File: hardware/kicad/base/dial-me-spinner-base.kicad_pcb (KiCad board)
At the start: 2 copper layers, 57.6 x 46 mm, 25 parts, among them J1 TYPE-C-31-M-12, J2 BATT, J3 LINK, Q1 BSS138DW, SW1 TS-1187A, U1 BQ25180YBGR, U2 USBLC6-2SC6

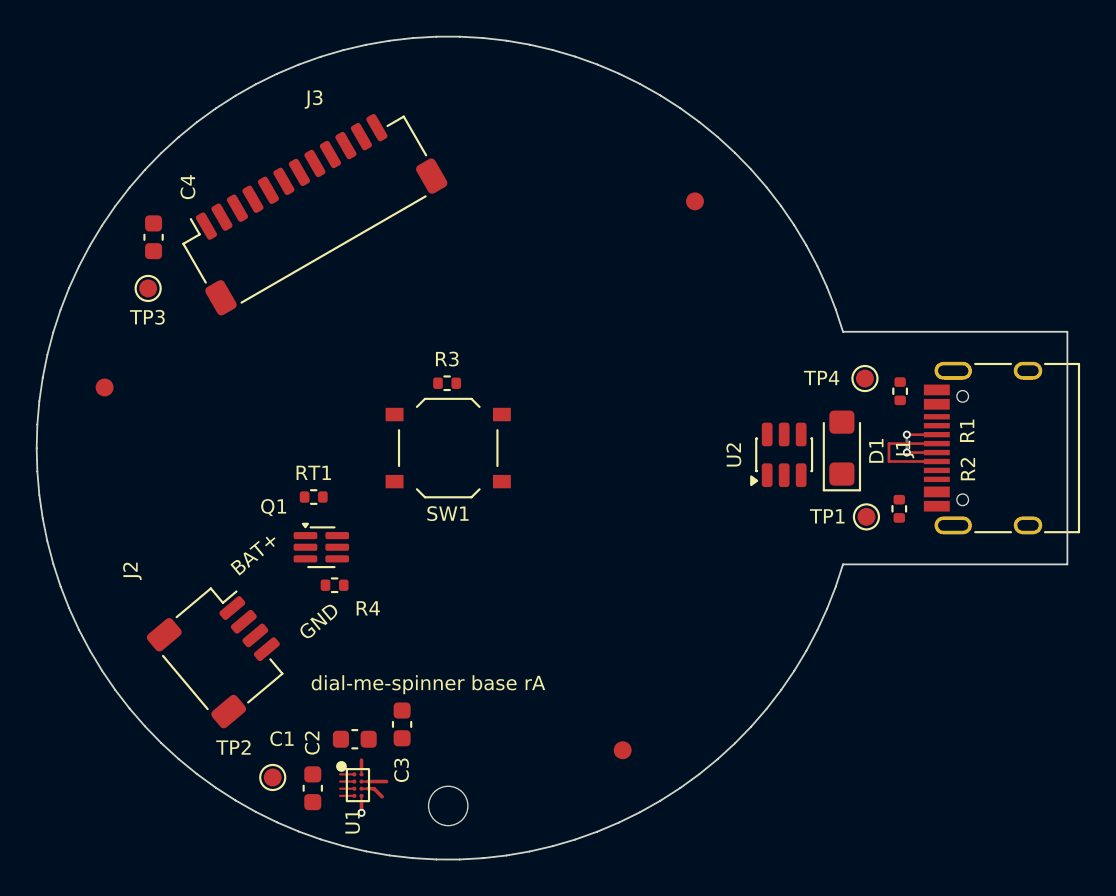
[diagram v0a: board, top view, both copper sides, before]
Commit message: NFC tag: P0.09/P0.10 as NFC1/NFC2 with 180 pF tuning caps and coil pads; CHG_INT_N moves to P1.03
Co-Authored-By: Claude Opus 5.5 <noreply@anthropic.com>
Claude-Session: https://claude.ai/code/session_01P3cqdBhxLcWY3sGUVf9LAJ
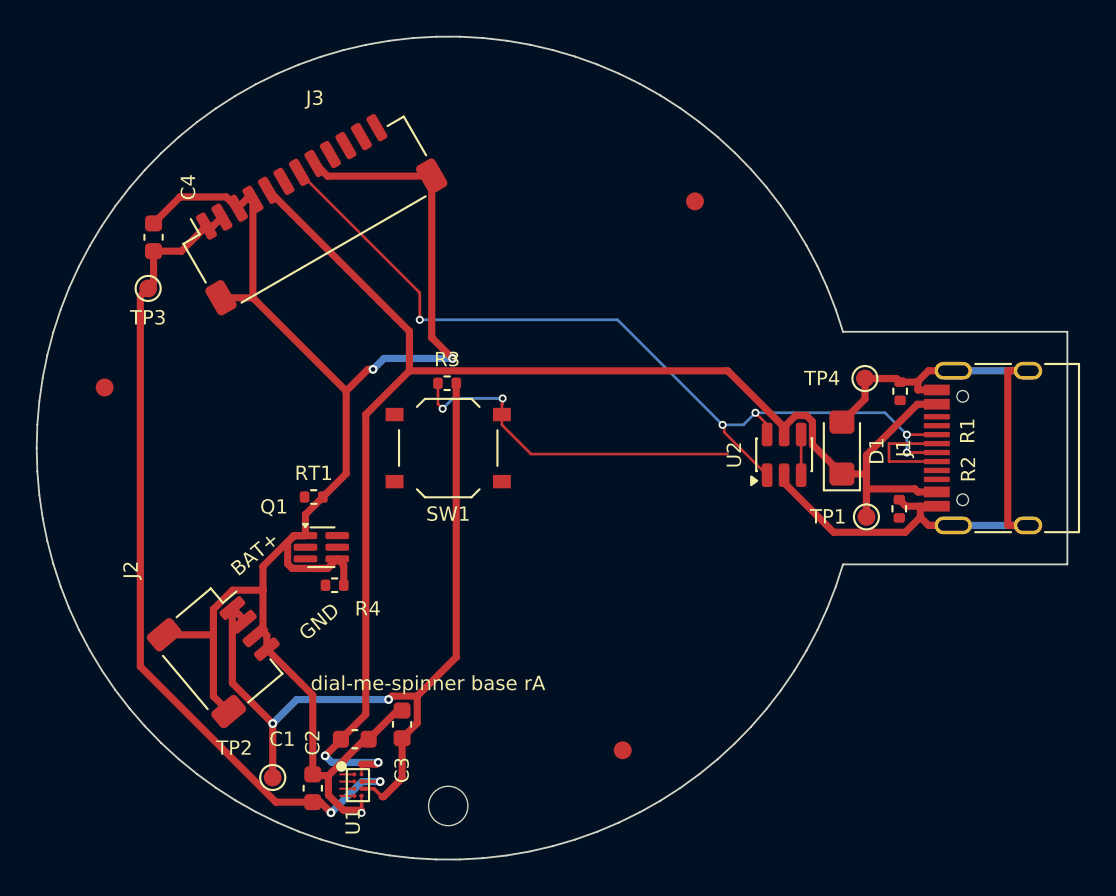
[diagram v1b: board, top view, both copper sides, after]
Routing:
- net GND: track 0.95 -> 144.2 mm, vias 1 -> 3
- net VBUS: track 0.80 -> 83.9 mm, vias 0 -> 2
- net /Base board/USB_DP: track 4.35 -> 51.2 mm, vias 2 -> 5
- net VSYS: track 1.40 -> 46.9 mm, vias 0 -> 2
- net VBAT: track 1.34 -> 46.6 mm, vias 0 -> 2
- net /Base board/SW_HI: track 0.00 -> 19.9 mm, vias 0 -> 2
- net /Base board/USB_DM: track 6.35 -> 8.63 mm

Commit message: WIP: SPICE tests and boards in progress
Co-Authored-By: Claude Opus 5.5 <noreply@anthropic.com>
Claude-Session: https://claude.ai/code/session_01P3cqdBhxLcWY3sGUVf9LAJ
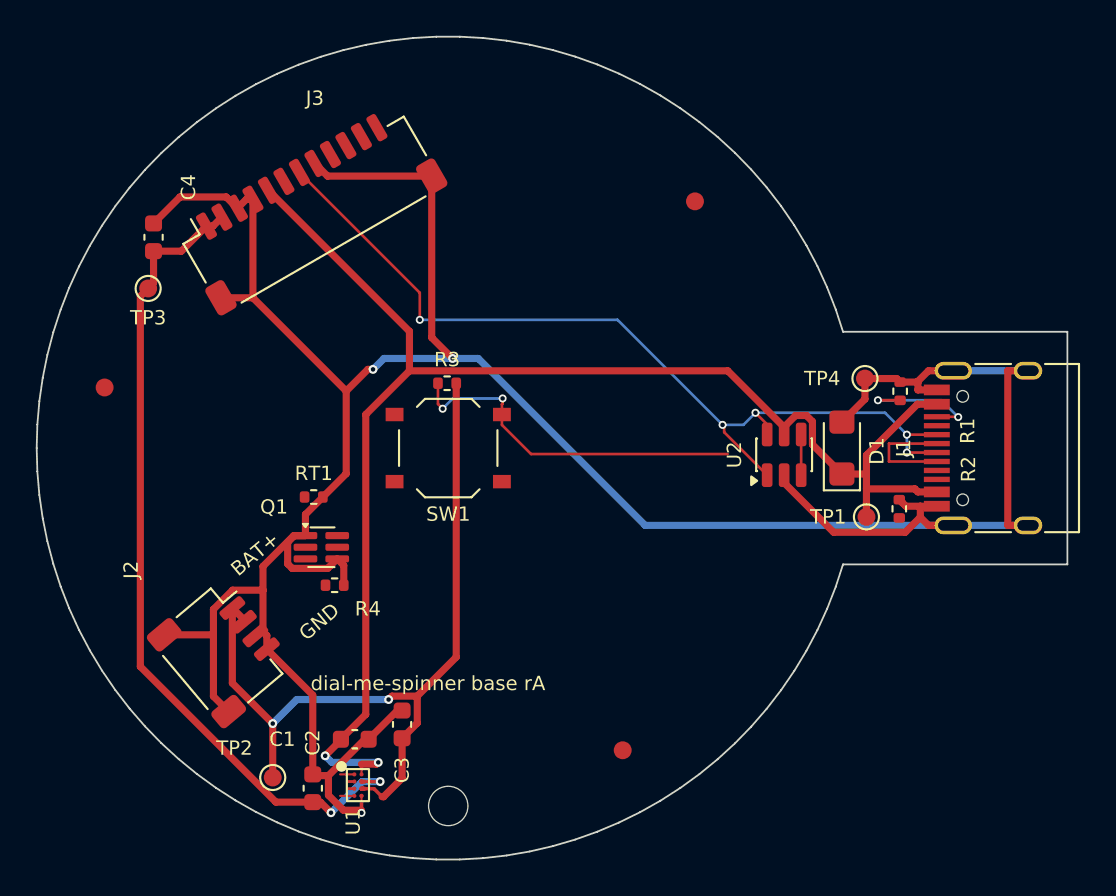
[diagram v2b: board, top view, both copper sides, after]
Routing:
- net GND: track 144.2 -> 176.3 mm
- net /Base board/USB_CC2: track 0.00 -> 7.32 mm, vias 0 -> 2
- net VBUS: track 83.9 -> 84.5 mm

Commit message: SPICE findings (sources): U21 QOD to OLED_VIN, R4 68R, R12 4R7, 25 V VSYS caps, base R4 100k, C1 0805 X7R
Netlists are regenerated once the last two SPICE verifications finish.

Co-Authored-By: Claude Opus 5.5 <noreply@anthropic.com>
Claude-Session: https://claude.ai/code/session_01P3cqdBhxLcWY3sGUVf9LAJ
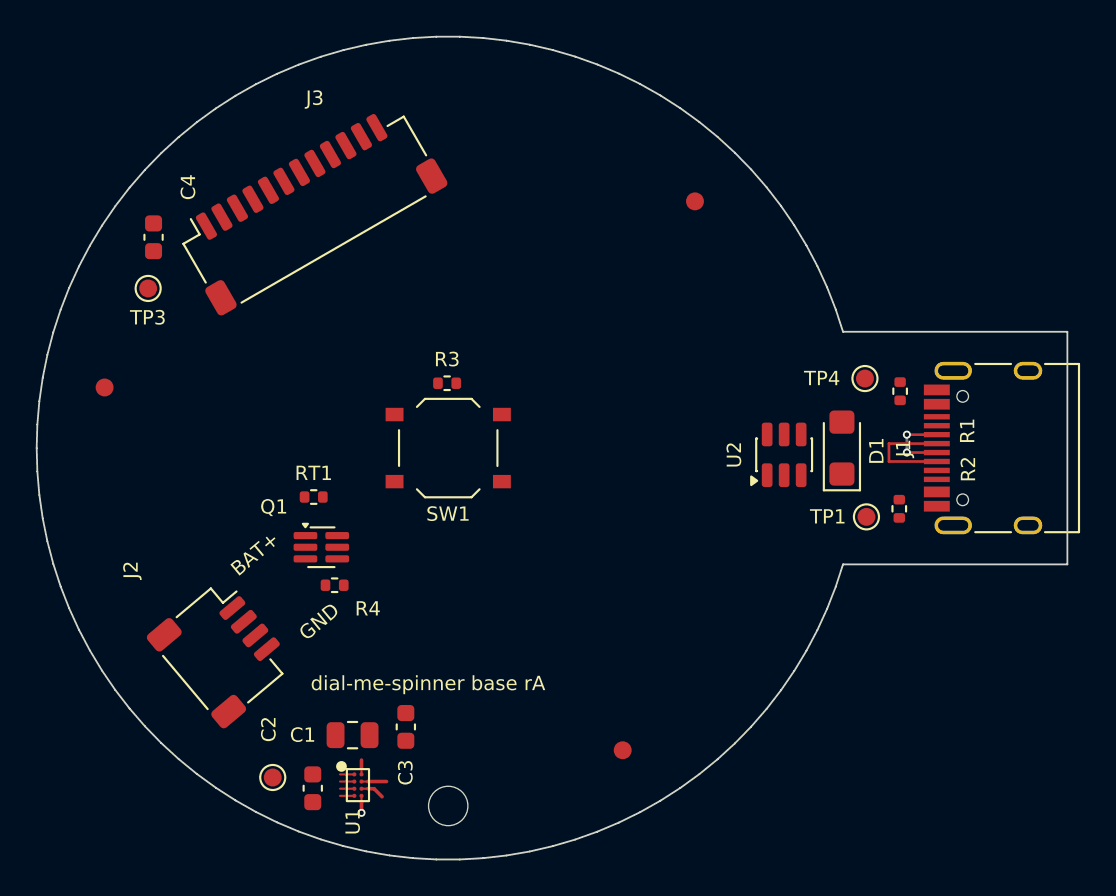
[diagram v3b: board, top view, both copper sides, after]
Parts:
- C1: footprint Capacitor_SMD:C_0603_1608Metric -> Capacitor_SMD:C_0805_2012Metric
- moved C1 0.26 mm to (94.7, 116.0)
- moved C3 0.25 mm to (97.6, 115.6)
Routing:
- net GND: track 176.3 -> 0.95 mm, vias 3 -> 1
- net VBUS: track 84.5 -> 0.80 mm, vias 2 -> 0
- net /Base board/USB_DP: track 51.2 -> 4.35 mm, vias 5 -> 2
- net VSYS: track 46.9 -> 1.40 mm, vias 2 -> 0
- net VBAT: track 46.7 -> 1.34 mm, vias 2 -> 0
- net /Base board/SW_HI: track 19.9 -> 0.00 mm, vias 2 -> 0
- net /Base board/USB_CC2: track 7.32 -> 0.00 mm, vias 2 -> 0
- net /Base board/USB_DM: track 8.63 -> 6.35 mm

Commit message: Base board goes 4-layer (In1 GND plane); fix In1 power-plane marking for KiCad 9 (layer id 4)
The 2-layer base never routed completely (J3 signals and the button/charger network had to
cross the power tracks with GND routed as tracks). set_layer_types matched '(1 "In1.Cu" ...)',
but KiCad 9 numbers In1 as layer 4, so the main board's GND plane was routed as a signal layer too.

Co-Authored-By: Claude Opus 5.5 <noreply@anthropic.com>
Claude-Session: https://claude.ai/code/session_01P3cqdBhxLcWY3sGUVf9LAJ
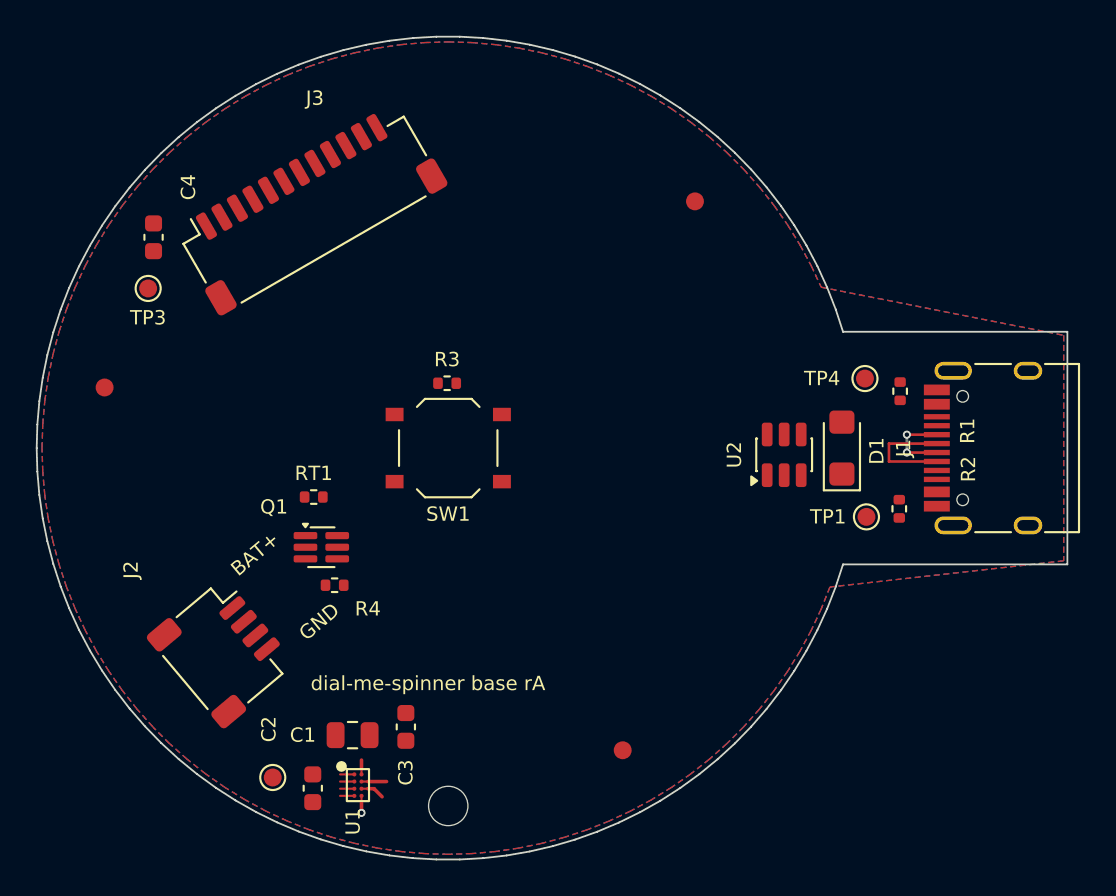
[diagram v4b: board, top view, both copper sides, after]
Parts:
- C4: value 10u -> 10u/25V
- R4: value 1M -> 100k
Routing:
- added copper zone on B.Cu, net GND
- added copper zone on F.Cu, net GND
- added copper zone on In1.Cu, net GND
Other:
- copper layers 2 -> 4

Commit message: WIP: SPICE verification and routing in progress
Co-Authored-By: Claude Opus 5.5 <noreply@anthropic.com>
Claude-Session: https://claude.ai/code/session_01P3cqdBhxLcWY3sGUVf9LAJ
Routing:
- removed copper zone on B.Cu, net GND
- removed copper zone on F.Cu, net GND

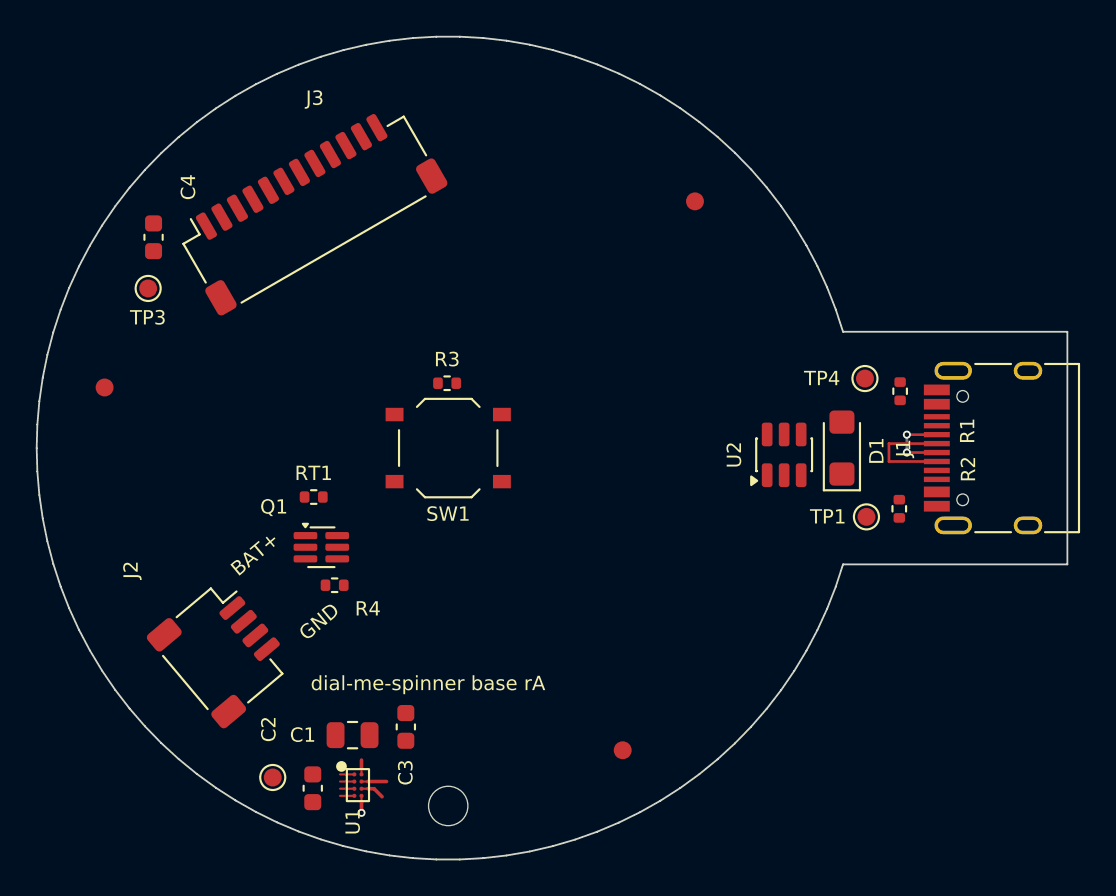
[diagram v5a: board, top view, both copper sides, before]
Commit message: Base board routed (4 layers): 0 unconnected, DRC clean with schematic parity; prune also removes bypassed escape stubs
Co-Authored-By: Claude Opus 5.5 <noreply@anthropic.com>
Claude-Session: https://claude.ai/code/session_01P3cqdBhxLcWY3sGUVf9LAJ
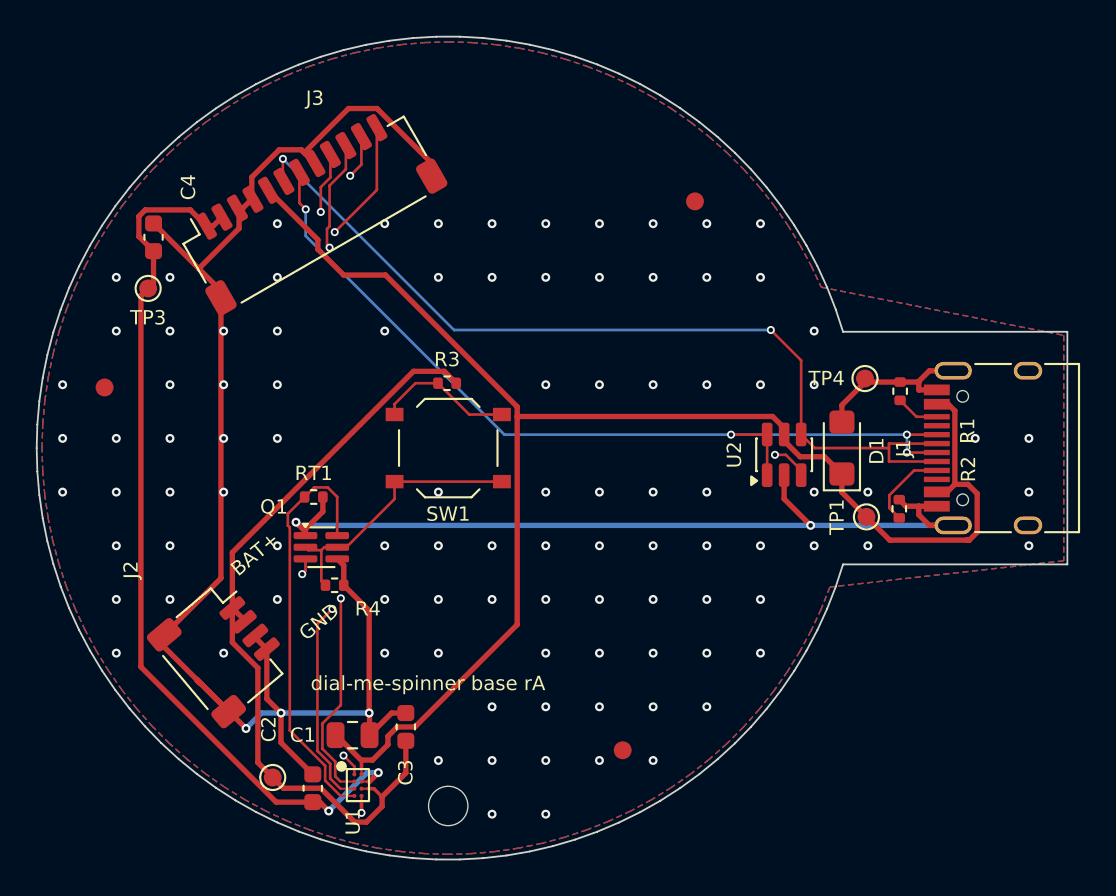
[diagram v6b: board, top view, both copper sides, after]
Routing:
- net GND: track 0.95 -> 180.9 mm, vias 1 -> 106
- net VBUS: track 0.80 -> 86.2 mm
- net /Base board/USB_DM: track 6.35 -> 59.8 mm, vias 0 -> 3
- net VSYS: track 1.40 -> 49.8 mm, vias 0 -> 2
- net /Base board/USB_DP: track 4.35 -> 50.5 mm, vias 2 -> 4
- net VBAT: track 1.34 -> 44.6 mm
- net /Base board/I2C_SDA: track 0.80 -> 38.2 mm, vias 0 -> 2
- net /Base board/I2C_SCL: track 0.80 -> 37.6 mm, vias 0 -> 2
- net /Base board/CHG_INT_N: track 0.80 -> 36.3 mm, vias 0 -> 2
- net /Base board/BTN_N: track 0.00 -> 27.7 mm, vias 0 -> 2
- net /Base board/CHG_TSMR: track 0.80 -> 23.5 mm
- net /Base board/SW_GATE: track 0.00 -> 15.3 mm
- net /Base board/SW_HI: track 0.00 -> 7.79 mm
- net /Base board/USB_CC1: track 0.00 -> 4.73 mm
- net /Base board/USB_CC2: track 0.00 -> 2.43 mm
- added copper zone on B.Cu, net GND
- added copper zone on F.Cu, net GND
